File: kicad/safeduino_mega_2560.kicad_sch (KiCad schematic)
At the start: 84 parts, among them X1 USBB-1J

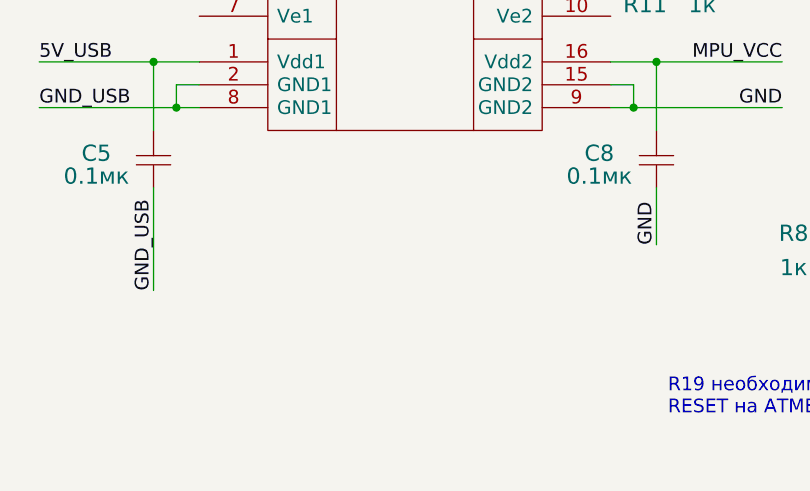
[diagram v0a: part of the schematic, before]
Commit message: Добавил схему BL7142WH для сравнения с ADUM1301.
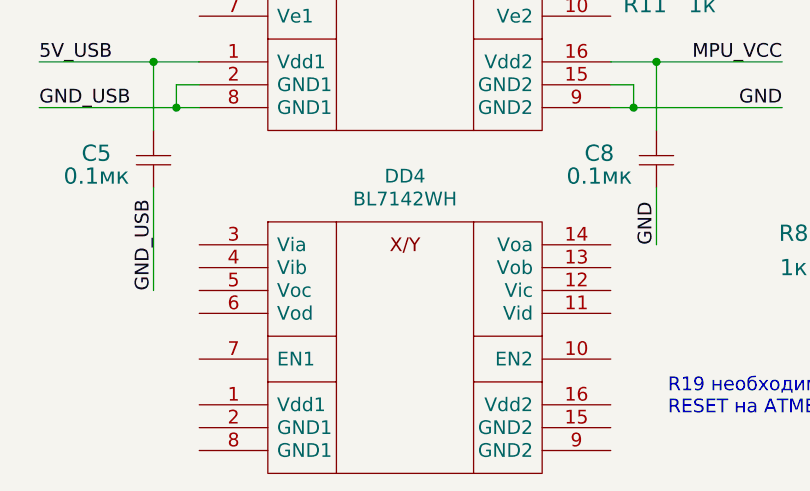
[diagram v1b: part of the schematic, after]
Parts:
- added DD4: BL7142WH, symbol IWconverter:BL7142WH
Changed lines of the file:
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@@
     (pin "2")
+  )
+  (symbol (lib_id "IWconverter:BL7142WH") (at 190.5 340.36 0) (unit 1)
+    (in_bom yes) (on_board yes)
+    (property "Reference" "DD4" (id 0) (at 205.74 335.28 0)
+      (effects (font (size 1.524 1.524)))
+    )
+    (property "Value" "BL7142WH" (id 1) (at 205.74 337.82 0)
+      (effects (font (size 1.524 1.524)))
+    )
+    (property "Footprint" "" (id 2) (at 190.5 340.36 0)
+      (effects (font (size 1.524 1.524)))
+    )
+    (property "Datasheet" "" (id 3) (at 190.5 340.36 0)
+      (effects (font (size 1.524 1.524)))
+    )
+    (pin "1")
+    (pin "10")
+    (pin "11")
+    (pin "12")
+    (pin "13")
+    (pin "14")
+    (pin "15")
+    (pin "16")
+    (pin "2")
+    (pin "3")
+    (pin "4")
+    (pin "5")
+    (pin "6")
+    (pin "7")
+    (pin "8")
+    (pin "9")
   )
   (sheet_instances
@@
       (reference "DD3") (unit 1) (value "ATMEGA2560-16AU") (footprint "IWsmd_case:TQFP100_case")
     )
+    (path "/088060cf-9440-4cf6-931d-fd6b401b5624"
+      (reference "DD4") (unit 1) (value "BL7142WH") (footprint "")
+    )
     (path "/00000000-0000-0000-0000-000061e41c7d"

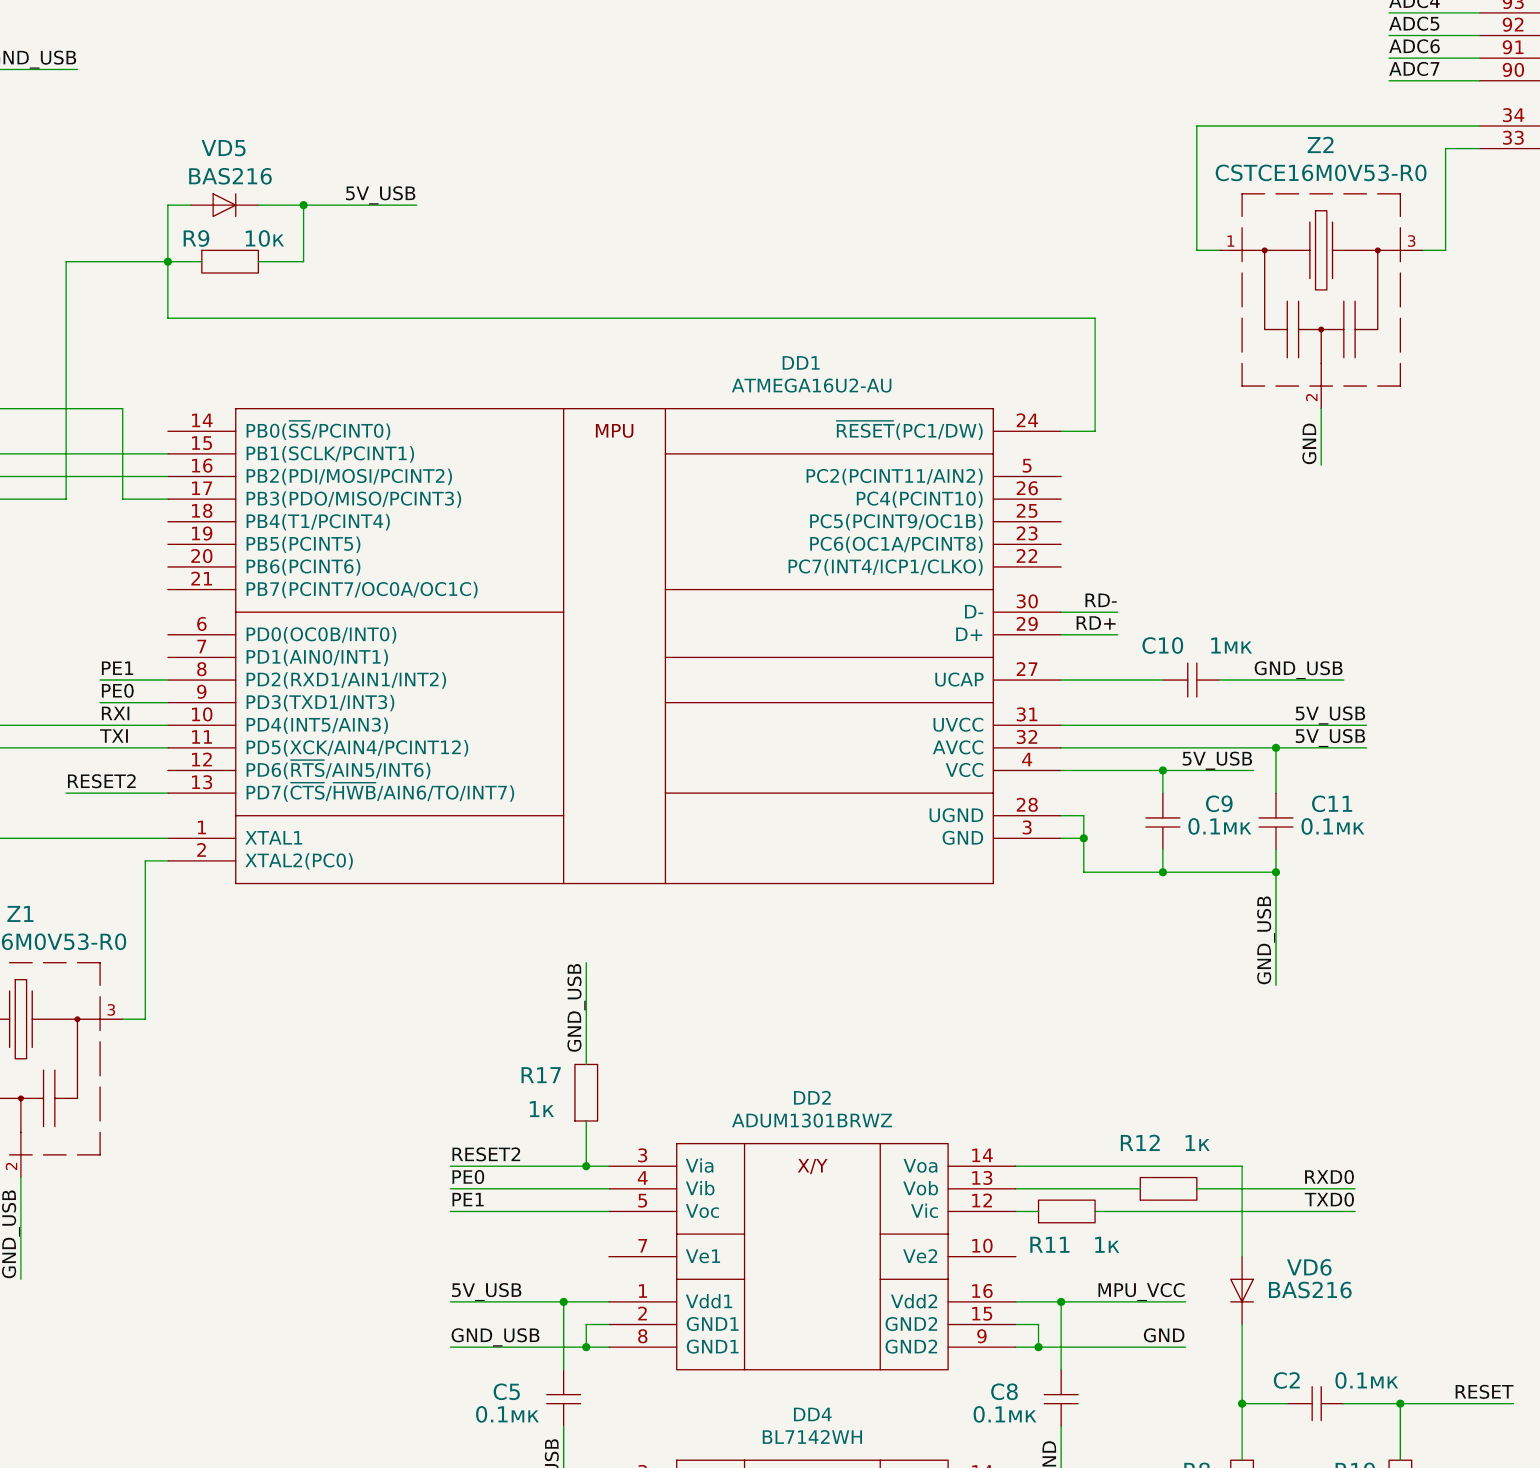
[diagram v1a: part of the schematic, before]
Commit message: Заменил посадочные места на SOD523 у VD5 и VD6.
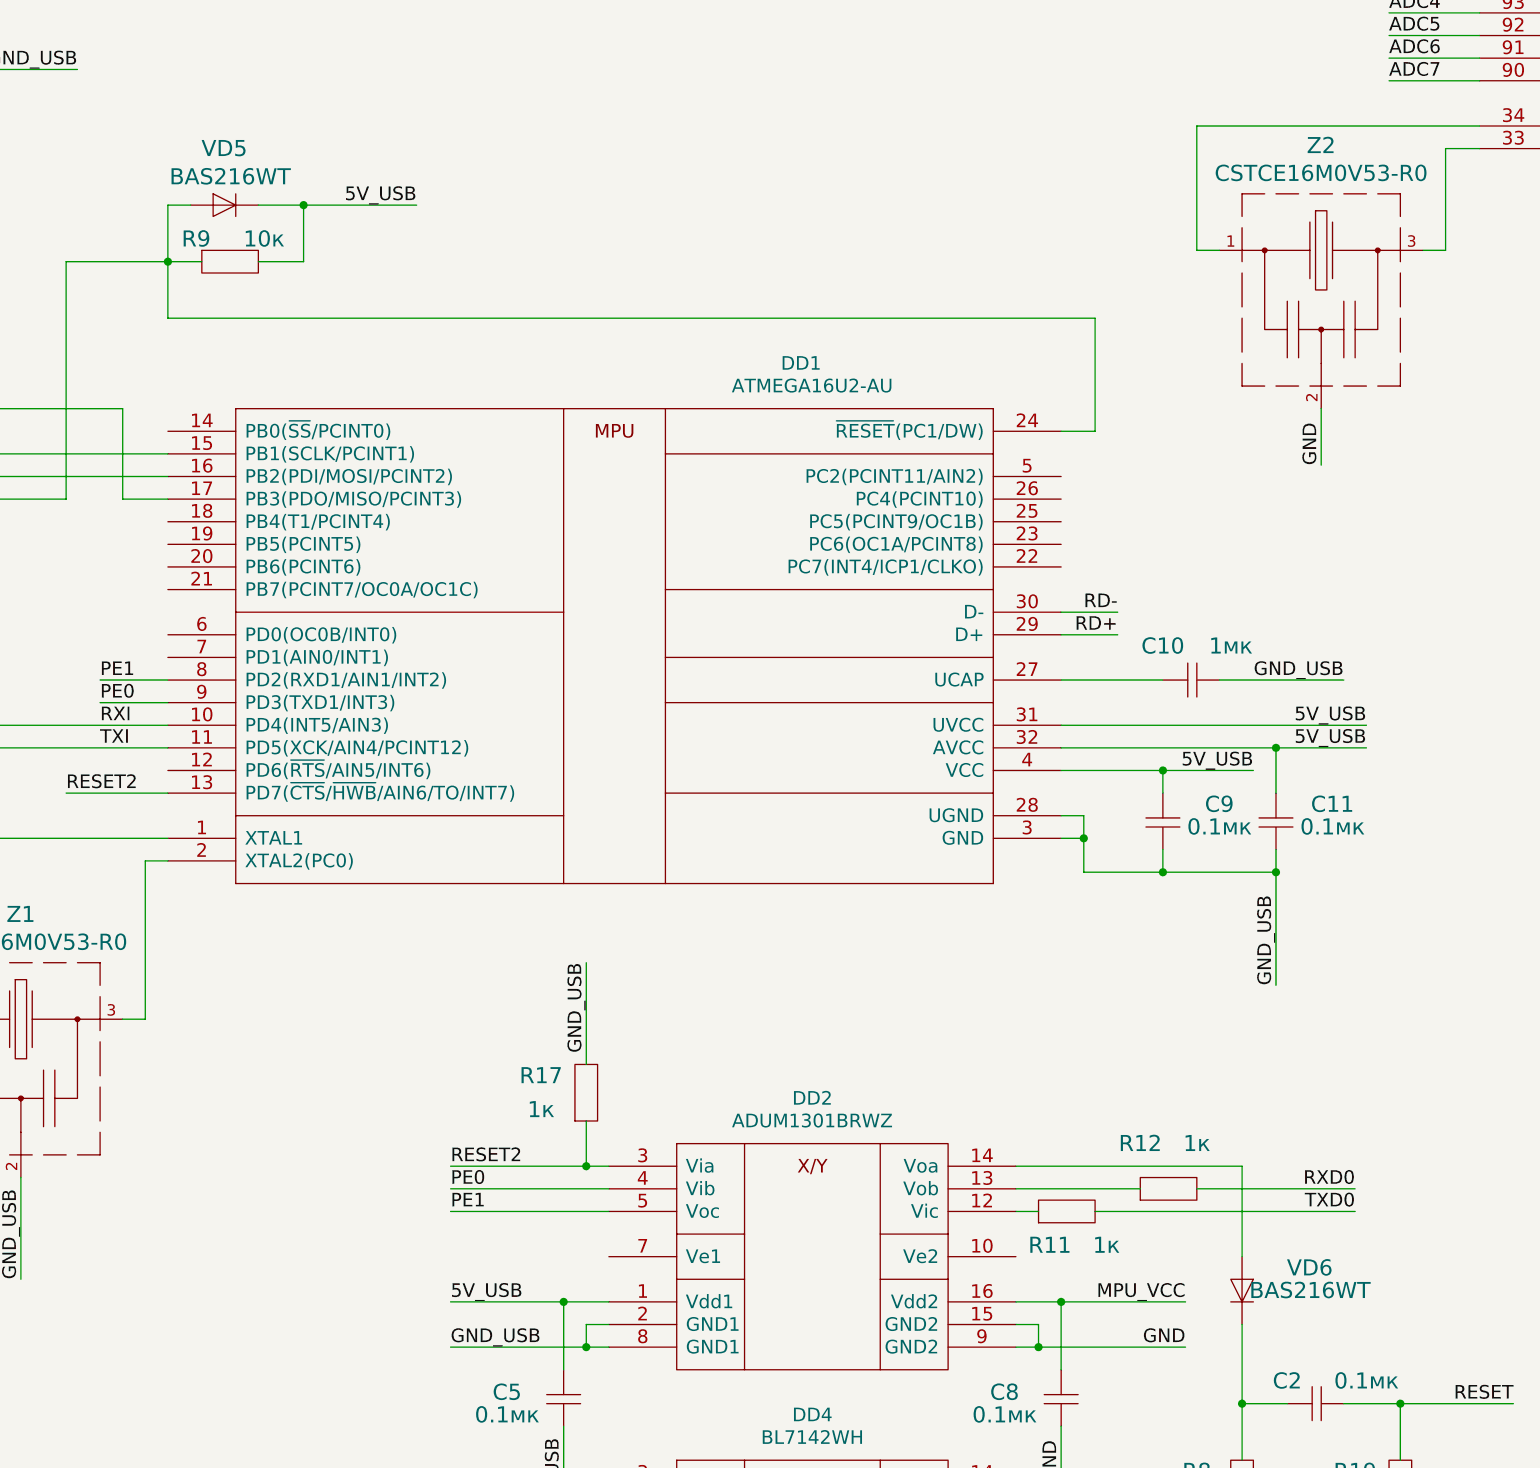
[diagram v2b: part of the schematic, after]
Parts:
- VD5, VD6: value BAS216 -> BAS216WT; footprint IWcomponents:SOD110 -> IWcomponents:SOD523
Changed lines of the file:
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@@
       (effects (font (size 1.8034 1.8034)))
     )
-    (property "Value" "BAS216" (id 1) (at 140.335 196.215 0)
-      (effects (font (size 1.8034 1.8034)))
-    )
-    (property "Footprint" "IWcomponents:SOD110" (id 2) (at 135.89 199.39 0)
+    (property "Value" "BAS216WT" (id 1) (at 140.335 196.215 0)
+      (effects (font (size 1.8034 1.8034)))
+    )
+    (property "Footprint" "IWcomponents:SOD523" (id 2) (at 135.89 199.39 0)
       (effects (font (size 1.524 1.524)) hide)
     )
@@
       (effects (font (size 1.8034 1.8034)))
     )
-    (property "Value" "BAS216" (id 1) (at 261.62 321.31 90)
-      (effects (font (size 1.8034 1.8034)))
-    )
-    (property "Footprint" "IWcomponents:SOD110" (id 2) (at 254 317.5 0)
+    (property "Value" "BAS216WT" (id 1) (at 261.62 321.31 90)
+      (effects (font (size 1.8034 1.8034)))
+    )
+    (property "Footprint" "IWcomponents:SOD523" (id 2) (at 254 317.5 0)
       (effects (font (size 1.524 1.524)) hide)
     )
@@
     )
     (property "Footprint" "" (id 2) (at 190.5 340.36 0)
-      (effects (font (size 1.524 1.524)))
+      (effects (font (size 1.524 1.524)) hide)
     )
     (property "Datasheet" "" (id 3) (at 190.5 340.36 0)
@@
     )
     (path "/00000000-0000-0000-0000-00005256a146"
-      (reference "VD5") (unit 1) (value "BAS216") (footprint "IWcomponents:SOD110")
+      (reference "VD5") (unit 1) (value "BAS216WT") (footprint "IWcomponents:SOD523")
     )
     (path "/00000000-0000-0000-0000-000056e17300"
-      (reference "VD6") (unit 1) (value "BAS216") (footprint "IWcomponents:SOD110")
+      (reference "VD6") (unit 1) (value "BAS216WT") (footprint "IWcomponents:SOD523")
     )
     (path "/00000000-0000-0000-0000-000064a3fcc7"

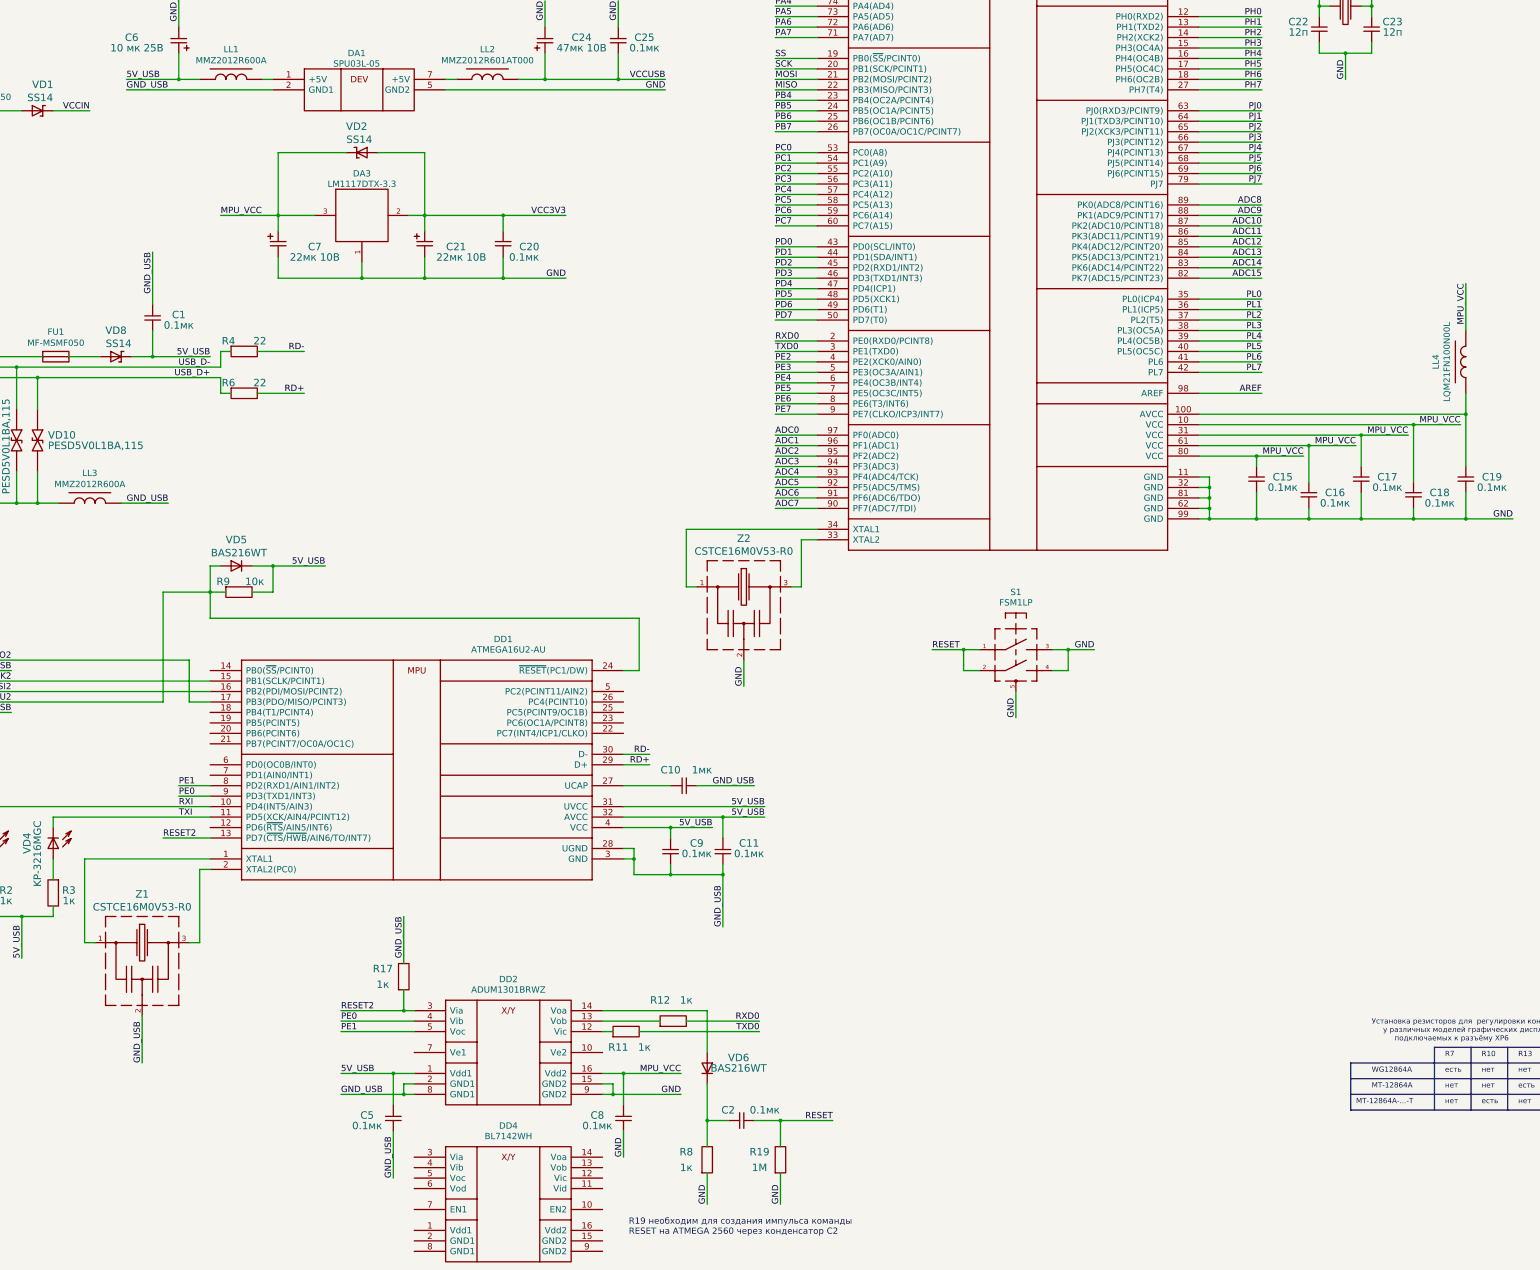
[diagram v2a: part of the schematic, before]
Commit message: Перевёл проект SafeDuino MEGA 2560 на Kicad 7.0 и поправил найденные недочёты на печатной плате.
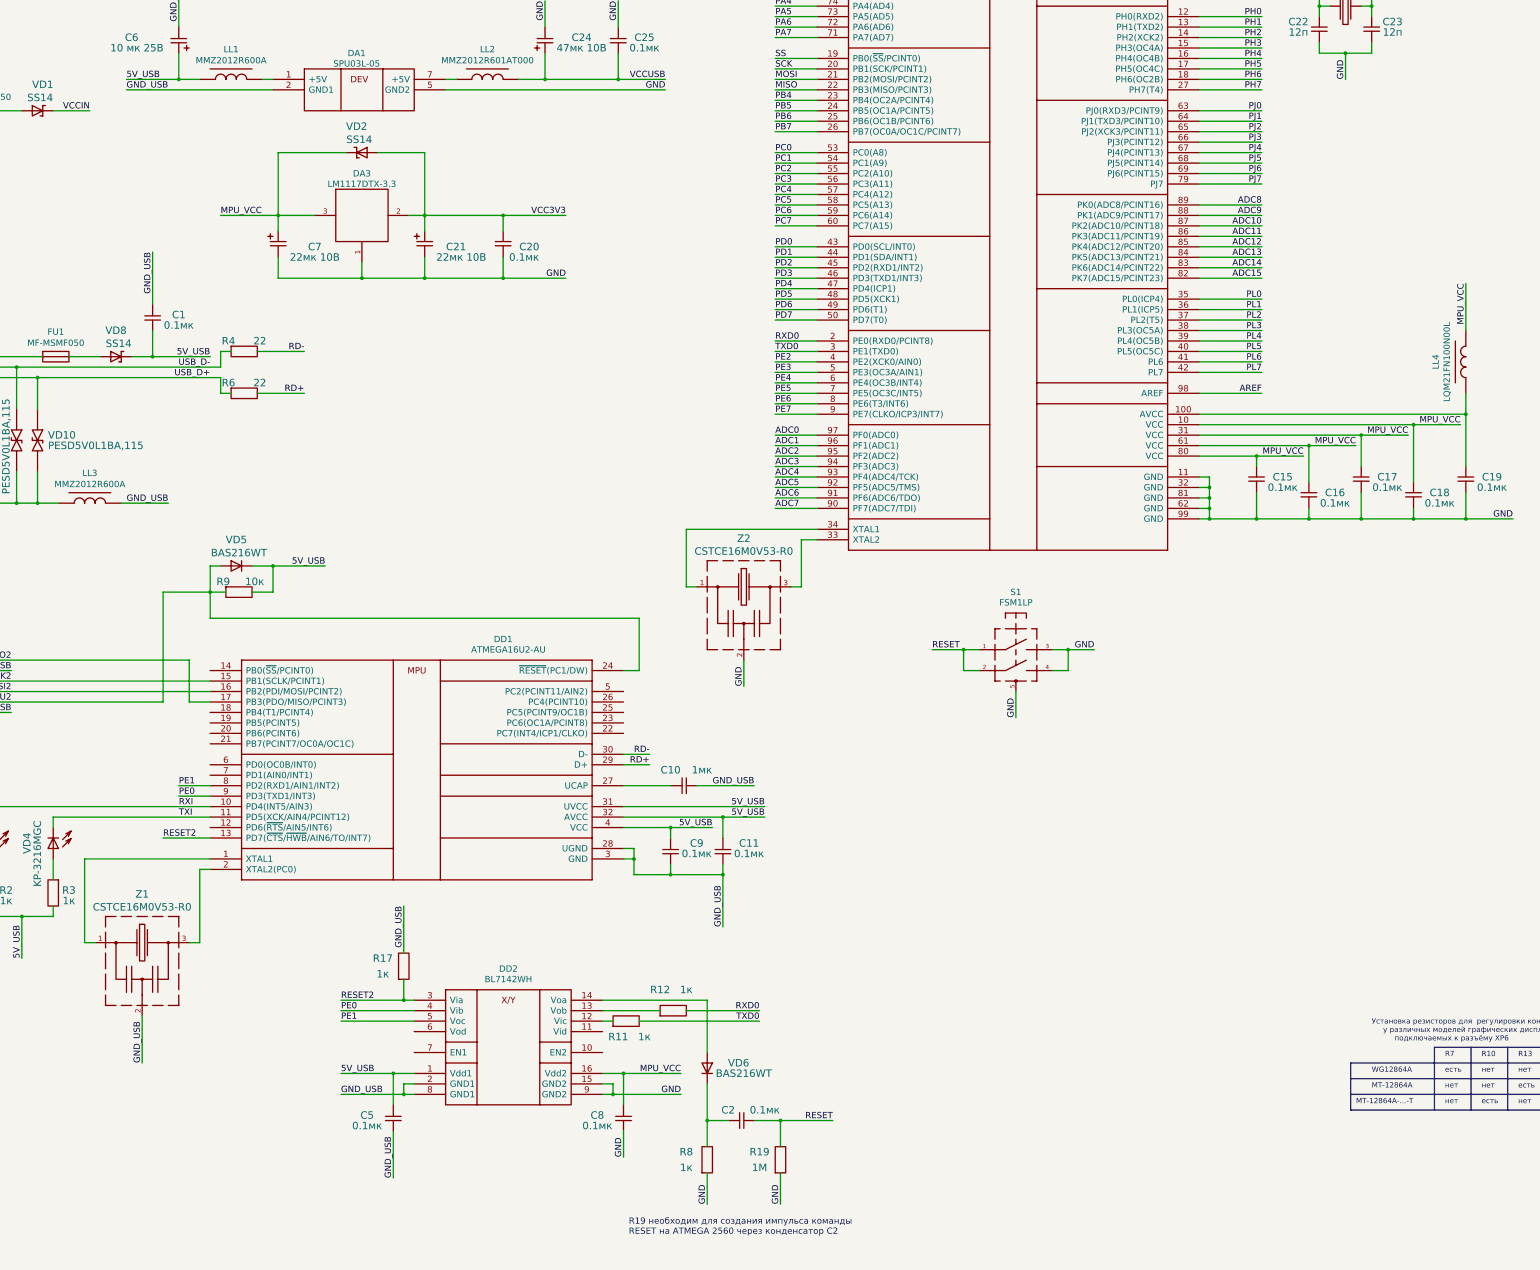
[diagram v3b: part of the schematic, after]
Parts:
- removed DD2: ADUM1301BRWZ, IWsmd_case:SOIC16_RW16, symbol LFcomponents:ADUM1301
- DA1: footprint IWcomponents:P10LU-0515ZLF -> IWcomponents:SIP-7_4pin
- DD2: renamed from DD4; footprint (none) -> IWsmd_case:SOIC16_RW16
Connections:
- net 5V_USB: now also DD2.1 (Vdd1)
- net GND: now also DD2.15 (GND2), DD2.9 (GND2)
- net GND_USB: now also DD2.2 (GND1), DD2.8 (GND1)
- net MPU_VCC: now also DD2.16 (Vdd2)
- net PE0: now also DD2.4 (Vib)
- net PE1: now also DD2.5 (Voc)
- net RESET2: now also DD2.3 (Via)
- net at R11.1: now also DD2.12 (Vic)
- net at R12.1: now also DD2.13 (Vob)
- net at VD6.1: now also DD2.14 (Voa)
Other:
- moved on the sheet: DD2, R11, R12, R17
